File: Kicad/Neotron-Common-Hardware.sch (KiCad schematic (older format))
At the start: 8 parts, among them J101 DB15_Female_HighDensity_Mount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, J102 AudioJack3, J103 DB9_Male_MountingHoles, J104 USB_B, J105 USB_A, J106 RJ45_Amphenol_RJMG1BD3B8K1ANR, J107 Double-mini-DIN-6

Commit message: Update notes on schematic.
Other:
- note added: "Atari/Commodore digital joystick interface.\nCan support SEGA MegaDrive/Genesis pads if\nyou put 5V on Pin 5, and a Select signal on pin 7.\n\nYou can also use an IDC 10-way box header along with\nan IDC 9-way socket on a ribbon. If so, Pin 10 is N/C."
- note added: "Ethernet Jack with integrated magnetics.\nGreen LED is Activity.\nYellow LED is 100base-T mode active."
- note added: "RS-232 9-pin Serial. Must have at least RX, TX, RTS and CTS\nconnected. Can optionally connect DTR, DSR, RI and CD.\n\nYou can also use an IDC 10-way box header along with\nan IDC 9-way plug on a ribbon. If so, Pin 10 is N/C."
- note added: "The USB Type-A port allows you to plug\nUSB keyboards, mice and other devices\ninto your Neotron.\n\nThe VBUS line is either connected to the main 5V\nline, or connected via a 500mA resettable fuse/switch\nso you can power-off misbehaving devices. See\nMIC2005."
- note added: "The VGA port. RGB is 0.7V p-p into 75 ohms. HSync and VSync is TTL.\nRecommend a 20MHz RGB video buffer to avoid overloading GPIO pins.\nSee TPF133A or THS7316."
- note removed: "Atari/Commodore digital joystick interface.\nCan support SEGA MegaDrive/Genesis pads if\nyou put 5V on Pin 5, and a Select signal on pin 7.\n\nYou can also use an IDC 10-way box header along with\nan IDC 9-way socket on a ribbon."
- note removed: "Ethernet Jack with integrated magnetics."
- note removed: "RS-232 9-pin Serial. Must have at least RX, TX, RTS and CTS\nconnected. Can optionally connect DTR, DSR, RI and CD.\n\nYou can also use an IDC 10-way box header along with\nan IDC 9-way plug on a ribbon."
- note removed: "The USB Type-A port allows you to plug\nUSB keyboards, mice and other devices\ninto your Neotron.\n\nThe VBUS line is either connected to the main 5V\nline, or connected via a 500mA resettable fuse/switch\nso you can power-off misbehaving devices."
- note removed: "The VGA port. RGB is 0.7V p-p into 75 ohms. HSync and VSync is TTL.\nRecommend a 20MHz RGB video buffer to avoid overloading GPIO pins."
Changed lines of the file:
@@
 $EndComp
 Text Notes 6400 2700 0    50   ~ 0
-The USB Type-A port allows you to plug\nUSB keyboards, mice and other devices\ninto your Neotron.\n\nThe VBUS line is either connected to the main 5V\nline, or connected via a 500mA resettable fuse/switch\nso you can power-off misbehaving devices.
+The USB Type-A port allows you to plug\nUSB keyboards, mice and other devices\ninto your Neotron.\n\nThe VBUS line is either connected to the main 5V\nline, or connected via a 500mA resettable fuse/switch\nso you can power-off misbehaving devices. See\nMIC2005.
 Text Notes 6400 1300 0    50   ~ 0
 The USB Type-B port is used as a 5V input for the system.\nYou could use a 2.51mm (inner, 5.5mm outer diameter) barrel\njack instead.
@@
 Stereo line-level audio. May not be suitable for headphones.\nIf your design has an amplified output, out that on a second\n3.5mm connector.
 Text Notes 7000 4200 0    50   ~ 0
-The VGA port. RGB is 0.7V p-p into 75 ohms. HSync and VSync is TTL.\nRecommend a 20MHz RGB video buffer to avoid overloading GPIO pins.
+The VGA port. RGB is 0.7V p-p into 75 ohms. HSync and VSync is TTL.\nRecommend a 20MHz RGB video buffer to avoid overloading GPIO pins.\nSee TPF133A or THS7316.
 Text Notes 6700 5200 0    50   ~ 0
 Dual mini-DIN 6 connectors for PS/2 Keyboard and PS/2 Mouse.\nSignalling is 5V open-collector, with pull-up required.
 Text Notes 2400 2200 0    50   ~ 0
-RS-232 9-pin Serial. Must have at least RX, TX, RTS and CTS\nconnected. Can optionally connect DTR, DSR, RI and CD.\n\nYou can also use an IDC 10-way box header along with\nan IDC 9-way plug on a ribbon.
+RS-232 9-pin Serial. Must have at least RX, TX, RTS and CTS\nconnected. Can optionally connect DTR, DSR, RI and CD.\n\nYou can also use an IDC 10-way box header along with\nan IDC 9-way plug on a ribbon. If so, Pin 10 is N/C.
 Text Notes 2500 4300 0    50   ~ 0
-Ethernet Jack with integrated magnetics.
+Ethernet Jack with integrated magnetics.\nGreen LED is Activity.\nYellow LED is 100base-T mode active.
 $Comp
 L Connector:DB9_Female_MountingHoles J?
@@
 $EndComp
 Text Notes 2400 6200 0    50   ~ 0
-Atari/Commodore digital joystick interface.\nCan support SEGA MegaDrive/Genesis pads if\nyou put 5V on Pin 5, and a Select signal on pin 7.\n\nYou can also use an IDC 10-way box header along with\nan IDC 9-way socket on a ribbon.
+Atari/Commodore digital joystick interface.\nCan support SEGA MegaDrive/Genesis pads if\nyou put 5V on Pin 5, and a Select signal on pin 7.\n\nYou can also use an IDC 10-way box header along with\nan IDC 9-way socket on a ribbon. If so, Pin 10 is N/C.
 $EndSCHEMATC

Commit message: Splitting into sub-modules.
Also started Audio jack connections.
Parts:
- removed J101: DB15_Female_HighDensity_MountingHoles, Connector_Dsub:DSUB-15-HD_Male_Horizontal_P2.29x1.98mm_EdgePinOffset3.03mm_Housed_MountingHolesOffset4.94mm, symbol Connector:DB15_Female_HighDensity_MountingHoles
- removed J102: AudioJack3, Connector_Audio:Jack_3.5mm_CUI_SJ1-3533NG_Horizontal, symbol Connector:AudioJack3
- removed J103: DB9_Male_MountingHoles, Connector_Dsub:DSUB-9_Male_Horizontal_P2.77x2.84mm_EdgePinOffset4.94mm_Housed_MountingHolesOffset7.48mm, symbol Connector:DB9_Male_MountingHoles
- removed J104: USB_B, Connector_USB:USB_B_OST_USB-B1HSxx_Horizontal, symbol Connector:USB_B
- removed J105: USB_A, Connector_USB:USB_A_Stewart_SS-52100-001_Horizontal, symbol Connector:USB_A
- removed J106: RJ45_Amphenol_RJMG1BD3B8K1ANR, Connector_RJ:RJ45_Amphenol_RJMG1BD3B8K1ANR, symbol Connector:RJ45_Amphenol_RJMG1BD3B8K1ANR
- removed J107: Double-mini-DIN-6, Neotron-Common-Hardware:Double_mini-DIN_6, symbol Neotron-Common-Hardware:Double-mini-DIN-6
- removed J?: DB9_Female_MountingHoles, symbol Connector:DB9_Female_MountingHoles
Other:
- note removed: "Atari/Commodore digital joystick interface.\nCan support SEGA MegaDrive/Genesis pads if\nyou put 5V on Pin 5, and a Select signal on pin 7.\n\nYou can also use an IDC 10-way box header along with\nan IDC 9-way socket on a ribbon. If so, Pin 10 is N/C."
- note removed: "Dual mini-DIN 6 connectors for PS/2 Keyboard and PS/2 Mouse.\nSignalling is 5V open-collector, with pull-up required."
- note removed: "Ethernet Jack with integrated magnetics.\nGreen LED is Activity.\nYellow LED is 100base-T mode active."
- note removed: "RS-232 9-pin Serial. Must have at least RX, TX, RTS and CTS\nconnected. Can optionally connect DTR, DSR, RI and CD.\n\nYou can also use an IDC 10-way box header along with\nan IDC 9-way plug on a ribbon. If so, Pin 10 is N/C."
- note removed: "Stereo line-level audio. May not be suitable for headphones.\nIf your design has an amplified output, out that on a second\n3.5mm connector."
- note removed: "The USB Type-A port allows you to plug\nUSB keyboards, mice and other devices\ninto your Neotron.\n\nThe VBUS line is either connected to the main 5V\nline, or connected via a 500mA resettable fuse/switch\nso you can power-off misbehaving devices. See\nMIC2005."
- note removed: "The USB Type-B port is used as a 5V input for the system.\nYou could use a 2.51mm (inner, 5.5mm outer diameter) barrel\njack instead."
- note removed: "The VGA port. RGB is 0.7V p-p into 75 ohms. HSync and VSync is TTL.\nRecommend a 20MHz RGB video buffer to avoid overloading GPIO pins.\nSee TPF133A or THS7316."
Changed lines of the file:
@@
 $Descr A4 11693 8268
 encoding utf-8
-Sheet 1 1
+Sheet 1 9
 Title ""
 Date ""
@@
 Comment4 ""
 $EndDescr
-$Comp
-L Connector:DB9_Male_MountingHoles J103
-U 1 1 5FCBF65F
-P 1600 2100
-F 0 "J103" V 1917 2056 50  0000 C CNN
-F 1 "DB9_Male_MountingHoles" V 1826 2056 50  0000 C CNN
-F 2 "Connector_Dsub:DSUB-9_Male_Horizontal_P2.77x2.84mm_EdgePinOffset4.94mm_Housed_MountingHolesOffset7.48mm" H 1600 2100 50  0001 C CNN
-F 3 " ~" H 1600 2100 50  0001 C CNN
-	1    1600 2100
-	0    -1   -1   0
-$EndComp
-$Comp
-L Connector:RJ45_Amphenol_RJMG1BD3B8K1ANR J106
-U 1 1 5FCC170E
-P 1600 4300
-F 0 "J106" V 1646 4888 50  0000 L CNN
-F 1 "RJ45_Amphenol_RJMG1BD3B8K1ANR" V 2585 3640 50  0000 L CNN
-F 2 "Connector_RJ:RJ45_Amphenol_RJMG1BD3B8K1ANR" H 1600 5000 50  0001 C CNN
-F 3 "https://www.amphenolcanada.com/ProductSearch/Drawings/AC/RJMG1BD3B8K1ANR.PDF" H 1600 5100 50  0001 C CNN
-	1    1600 4300
-	0    -1   -1   0
-$EndComp
-$Comp
-L Connector:AudioJack3 J102
-U 1 1 5FCC9839
-P 6000 3400
-F 0 "J102" H 5982 3725 50  0000 C CNN
-F 1 "AudioJack3" H 5982 3634 50  0000 C CNN
-F 2 "Connector_Audio:Jack_3.5mm_CUI_SJ1-3533NG_Horizontal" H 6000 3400 50  0001 C CNN
-F 3 "~" H 6000 3400 50  0001 C CNN
-	1    6000 3400
-	1    0    0    -1
-$EndComp
-$Comp
-L Connector:USB_A J105
-U 1 1 5FCCA16F
-P 5900 2470
-F 0 "J105" H 5957 2937 50  0000 C CNN
-F 1 "USB_A" H 5957 2846 50  0000 C CNN
-F 2 "Connector_USB:USB_A_Stewart_SS-52100-001_Horizontal" H 6050 2420 50  0001 C CNN
-F 3 " ~" H 6050 2420 50  0001 C CNN
-	1    5900 2470
-	1    0    0    -1
-$EndComp
-$Comp
-L Connector:USB_B J104
-U 1 1 5FCCAB69
-P 5900 1300
-F 0 "J104" H 5957 1767 50  0000 C CNN
-F 1 "USB_B" H 5957 1676 50  0000 C CNN
-F 2 "Connector_USB:USB_B_OST_USB-B1HSxx_Horizontal" H 6050 1250 50  0001 C CNN
-F 3 " ~" H 6050 1250 50  0001 C CNN
-	1    5900 1300
-	1    0    0    -1
-$EndComp
-$Comp
-L Connector:DB15_Female_HighDensity_MountingHoles J101
-U 1 1 5FCCD62D
-P 6000 4100
-F 0 "J101" V 6046 4829 50  0000 L CNN
-F 1 "DB15_Female_HighDensity_MountingHoles" V 5575 3480 50  0000 L CNN
-F 2 "Connector_Dsub:DSUB-15-HD_Male_Horizontal_P2.29x1.98mm_EdgePinOffset3.03mm_Housed_MountingHolesOffset4.94mm" H 5050 4500 50  0001 C CNN
-F 3 " ~" H 5050 4500 50  0001 C CNN
-	1    6000 4100
-	0    -1   -1   0
-$EndComp
-$Comp
-L Neotron-Common-Hardware:Double-mini-DIN-6 J107
-U 1 1 5FCD0B49
-P 6000 5500
-F 0 "J107" H 6000 6198 50  0000 C CNN
-F 1 "Double-mini-DIN-6" H 6000 6107 50  0000 C CNN
-F 2 "Neotron-Common-Hardware:Double_mini-DIN_6" H 6000 5750 50  0001 C CNN
-F 3 "http://www.mouser.com/ds/2/18/40_c091_abd_e-75918.pdf" H 6000 5750 50  0001 C CNN
-	1    6000 5500
-	1    0    0    -1
-$EndComp
-Text Notes 6400 2700 0    50   ~ 0
-The USB Type-A port allows you to plug\nUSB keyboards, mice and other devices\ninto your Neotron.\n\nThe VBUS line is either connected to the main 5V\nline, or connected via a 500mA resettable fuse/switch\nso you can power-off misbehaving devices. See\nMIC2005.
-Text Notes 6400 1300 0    50   ~ 0
-The USB Type-B port is used as a 5V input for the system.\nYou could use a 2.51mm (inner, 5.5mm outer diameter) barrel\njack instead.
-Text Notes 6400 3400 0    50   ~ 0
-Stereo line-level audio. May not be suitable for headphones.\nIf your design has an amplified output, out that on a second\n3.5mm connector.
-Text Notes 7000 4200 0    50   ~ 0
-The VGA port. RGB is 0.7V p-p into 75 ohms. HSync and VSync is TTL.\nRecommend a 20MHz RGB video buffer to avoid overloading GPIO pins.\nSee TPF133A or THS7316.
-Text Notes 6700 5200 0    50   ~ 0
-Dual mini-DIN 6 connectors for PS/2 Keyboard and PS/2 Mouse.\nSignalling is 5V open-collector, with pull-up required.
-Text Notes 2400 2200 0    50   ~ 0
-RS-232 9-pin Serial. Must have at least RX, TX, RTS and CTS\nconnected. Can optionally connect DTR, DSR, RI and CD.\n\nYou can also use an IDC 10-way box header along with\nan IDC 9-way plug on a ribbon. If so, Pin 10 is N/C.
-Text Notes 2500 4300 0    50   ~ 0
-Ethernet Jack with integrated magnetics.\nGreen LED is Activity.\nYellow LED is 100base-T mode active.
-$Comp
-L Connector:DB9_Female_MountingHoles J?
-U 1 1 5FD5B463
-P 1500 6100
-F 0 "J?" V 1817 6056 50  0000 C CNN
-F 1 "DB9_Female_MountingHoles" V 1726 6056 50  0000 C CNN
-F 2 "" H 1500 6100 50  0001 C CNN
-F 3 " ~" H 1500 6100 50  0001 C CNN
-	1    1500 6100
-	0    -1   -1   0
-$EndComp
-Text Notes 2400 6200 0    50   ~ 0
-Atari/Commodore digital joystick interface.\nCan support SEGA MegaDrive/Genesis pads if\nyou put 5V on Pin 5, and a Select signal on pin 7.\n\nYou can also use an IDC 10-way box header along with\nan IDC 9-way socket on a ribbon. If so, Pin 10 is N/C.
+$Sheet
+S 2500 2000 1000 1000
+U 5FDE658D
+F0 "Video" 50
+F1 "video.sch" 50
+$EndSheet
+$Sheet
+S 2500 3500 1000 1000
+U 5FDE698D
+F0 "Ethernet" 50
+F1 "ethernet.sch" 50
+$EndSheet
+$Sheet
+S 4000 2000 1000 1000
+U 5FDE6C5A
+F0 "Audio" 50
+F1 "audio.sch" 50
+$EndSheet
+$Sheet
+S 4000 3500 1000 1000
+U 5FDE7004
+F0 "USB" 50
+F1 "usb.sch" 50
+$EndSheet
+$Sheet
+S 5500 2000 1000 1000
+U 5FDE7599
+F0 "Power Supply" 50
+F1 "powersupply.sch" 50
+$EndSheet
+$Sheet
+S 5500 3500 1000 1000
+U 5FDEDE75
+F0 "PS/2 Keyboard and Mouse" 50
+F1 "ps2.sch" 50
+$EndSheet
+$Sheet
+S 5500 5000 1000 1000
+U 5FDF53DB
+F0 "Serial" 50
+F1 "serial.sch" 50
+$EndSheet
+$Sheet
+S 4000 5000 1000 1000
+U 5FDF58B0
+F0 "Joysticks" 50
+F1 "joysticks.sch" 50
+$EndSheet
 $EndSCHEMATC

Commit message: Completed Audio sheet.
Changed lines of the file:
@@
 Sheet 1 9
 Title ""
-Date ""
+Date "2020-12-20"
 Rev ""
-Comp ""
-Comment1 ""
-Comment2 ""
+Comp "https://neotron-compute.github.io/"
+Comment1 "Licenced as CC BY-SA"
+Comment2 "Copyright (c) The Neotron Developers, 2020"
 Comment3 ""
 Comment4 ""
@@
 $EndSheet
 $Sheet
-S 4000 2000 1000 1000
+S 4000 2000 1100 1000
 U 5FDE6C5A
 F0 "Audio" 50
 F1 "audio.sch" 50
+F2 "AUDIO_DAT_TO_CODEC" I L 4000 2100 50
+F3 "AUDIO_LR_TO_CODEC" I L 4000 2200 50
+F4 "AUDIO_BIT_CLK_TO_CODEC" I L 4000 2300 50
+F5 "AUDIO_DAT_FROM_CODEC" O L 4000 2400 50
+F6 "AUDIO_LR_FROM_CODEC" O L 4000 2500 50
+F7 "I2C_SDA" B L 4000 2600 50
+F8 "I2C_SCL" I L 4000 2700 50
 $EndSheet
 $Sheet

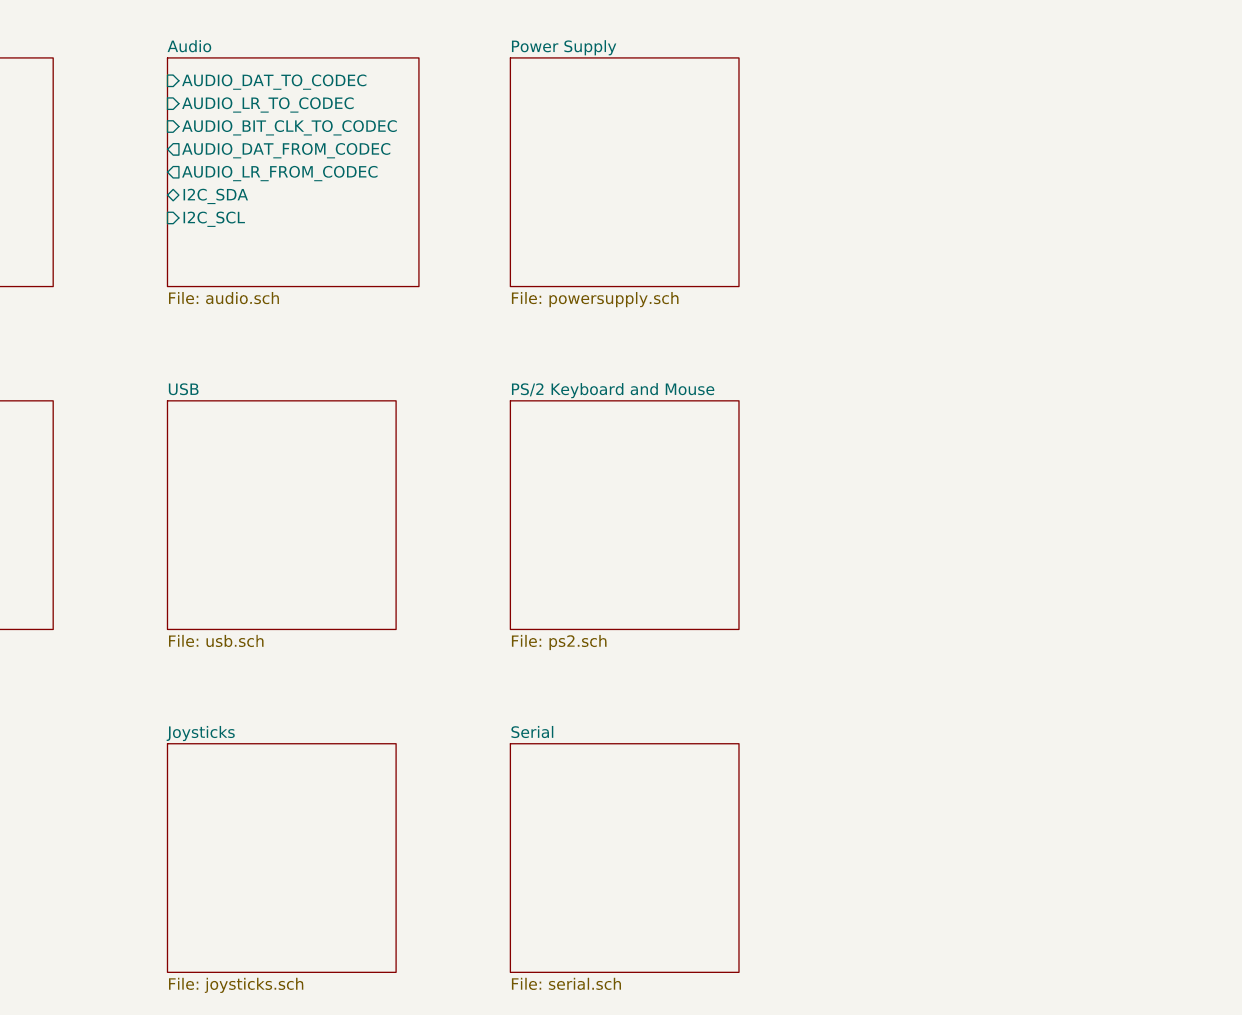
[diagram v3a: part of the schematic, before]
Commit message: Brought in RS232 circuit from Neotron 32.
Also updated 3D models.
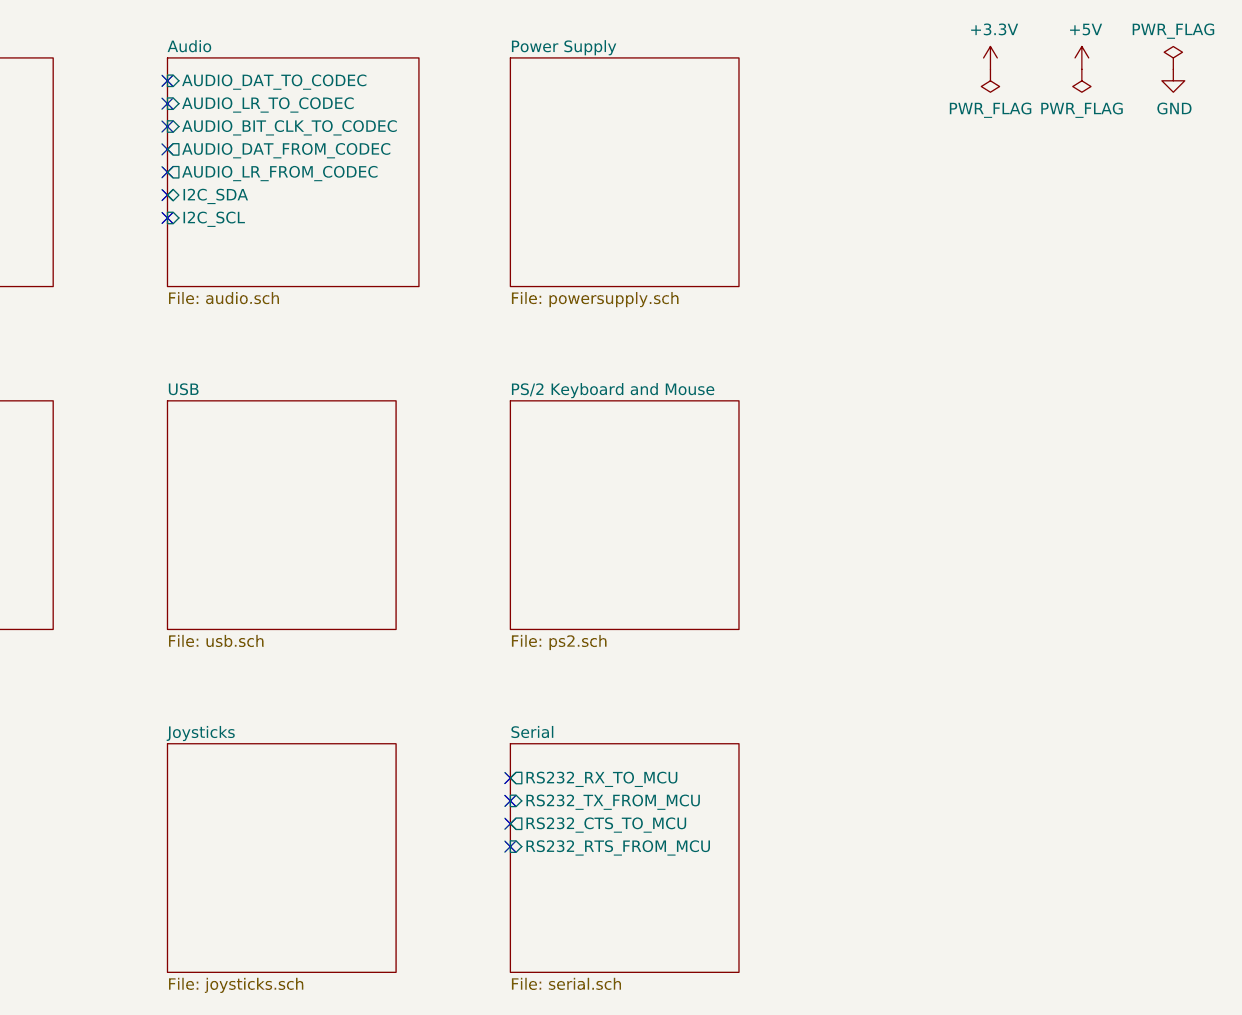
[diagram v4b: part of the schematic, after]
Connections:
- no-connect marks 0 -> 11
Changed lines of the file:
@@
 F0 "Serial" 50
 F1 "serial.sch" 50
+F2 "RS232_TX_FROM_MCU" I L 5500 5250 50
+F3 "RS232_RX_TO_MCU" O L 5500 5150 50
+F4 "RS232_RTS_FROM_MCU" I L 5500 5450 50
+F5 "RS232_CTS_TO_MCU" O L 5500 5350 50
 $EndSheet
 $Sheet
@@
 F1 "joysticks.sch" 50
 $EndSheet
+$Comp
+L power:+3.3V #PWR0101
+U 1 1 60A59BC0
+P 7600 2050
+F 0 "#PWR0101" H 7600 1900 50  0001 C CNN
+F 1 "+3.3V" H 7615 2223 50  0000 C CNN
+F 2 "" H 7600 2050 50  0001 C CNN
+F 3 "" H 7600 2050 50  0001 C CNN
+	1    7600 2050
+	1    0    0    -1
+$EndComp
+$Comp
+L power:+5V #PWR0102
+U 1 1 60A5A21B
+P 8000 2050
+F 0 "#PWR0102" H 8000 1900 50  0001 C CNN
+F 1 "+5V" H 8015 2223 50  0000 C CNN
+F 2 "" H 8000 2050 50  0001 C CNN
+F 3 "" H 8000 2050 50  0001 C CNN
+	1    8000 2050
+	1    0    0    -1
+$EndComp
+$Comp
+L power:GND #PWR0103
+U 1 1 60A5AA95
+P 8400 2050
+F 0 "#PWR0103" H 8400 1800 50  0001 C CNN
+F 1 "GND" H 8405 1877 50  0000 C CNN
+F 2 "" H 8400 2050 50  0001 C CNN
+F 3 "" H 8400 2050 50  0001 C CNN
+	1    8400 2050
+	1    0    0    -1
+$EndComp
+$Comp
+L power:PWR_FLAG #FLG0101
+U 1 1 60A5B22E
+P 8400 2050
+F 0 "#FLG0101" H 8400 2125 50  0001 C CNN
+F 1 "PWR_FLAG" H 8400 2223 50  0000 C CNN
+F 2 "" H 8400 2050 50  0001 C CNN
+F 3 "~" H 8400 2050 50  0001 C CNN
+	1    8400 2050
+	1    0    0    -1
+$EndComp
+$Comp
+L power:PWR_FLAG #FLG0102
+U 1 1 60A5B443
+P 8000 2050
+F 0 "#FLG0102" H 8000 2125 50  0001 C CNN
+F 1 "PWR_FLAG" H 8000 2223 50  0000 C CNN
+F 2 "" H 8000 2050 50  0001 C CNN
+F 3 "~" H 8000 2050 50  0001 C CNN
+	1    8000 2050
+	-1   0    0    1
+$EndComp
+$Comp
+L power:PWR_FLAG #FLG0103
+U 1 1 60A5BC87
+P 7600 2050
+F 0 "#FLG0103" H 7600 2125 50  0001 C CNN
+F 1 "PWR_FLAG" H 7600 2223 50  0000 C CNN
+F 2 "" H 7600 2050 50  0001 C CNN
+F 3 "~" H 7600 2050 50  0001 C CNN
+	1    7600 2050
+	-1   0    0    1
+$EndComp
+NoConn ~ 4000 2100
+NoConn ~ 4000 2200
+NoConn ~ 4000 2300
+NoConn ~ 4000 2400
+NoConn ~ 4000 2500
+NoConn ~ 4000 2600
+NoConn ~ 4000 2700
+NoConn ~ 5500 5150
+NoConn ~ 5500 5250
+NoConn ~ 5500 5350
+NoConn ~ 5500 5450
 $EndSCHEMATC

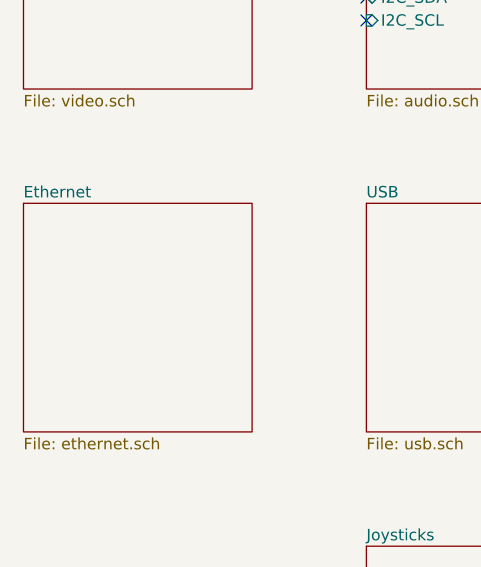
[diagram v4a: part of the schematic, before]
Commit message: Wired up Ethernet sheet.
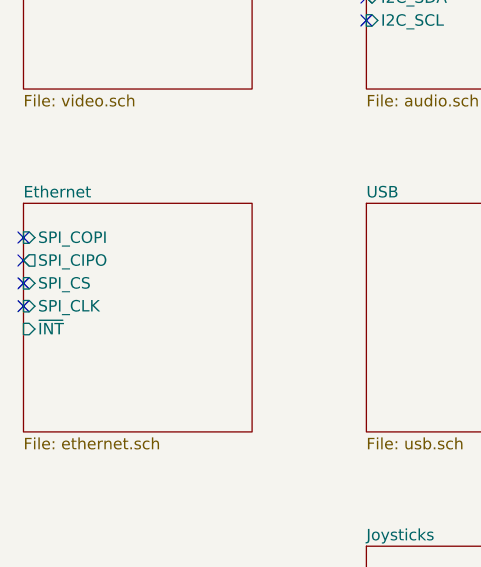
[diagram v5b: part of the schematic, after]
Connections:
- no-connect marks 11 -> 15
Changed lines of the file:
@@
 encoding utf-8
 Sheet 1 9
-Title ""
-Date "2020-12-20"
+Title "Neotron Common Hardware"
+Date "2020-12-22"
 Rev ""
 Comp "https://neotron-compute.github.io/"
@@
 F0 "Ethernet" 50
 F1 "ethernet.sch" 50
+F2 "SPI_COPI" I L 2500 3650 50
+F3 "SPI_CIPO" O L 2500 3750 50
+F4 "SPI_CS" I L 2500 3850 50
+F5 "SPI_CLK" I L 2500 3950 50
+F6 "~INT" I L 2500 4050 50
 $EndSheet
 $Sheet
@@
 NoConn ~ 5500 5350
 NoConn ~ 5500 5450
+NoConn ~ 2500 3750
+NoConn ~ 2500 3850
+NoConn ~ 2500 3950
+NoConn ~ 2500 3650
 $EndSCHEMATC
